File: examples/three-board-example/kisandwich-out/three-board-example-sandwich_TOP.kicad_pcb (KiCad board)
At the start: 6 copper layers, 55 x 55.8 mm, 1 part, among them U2 LM555xM

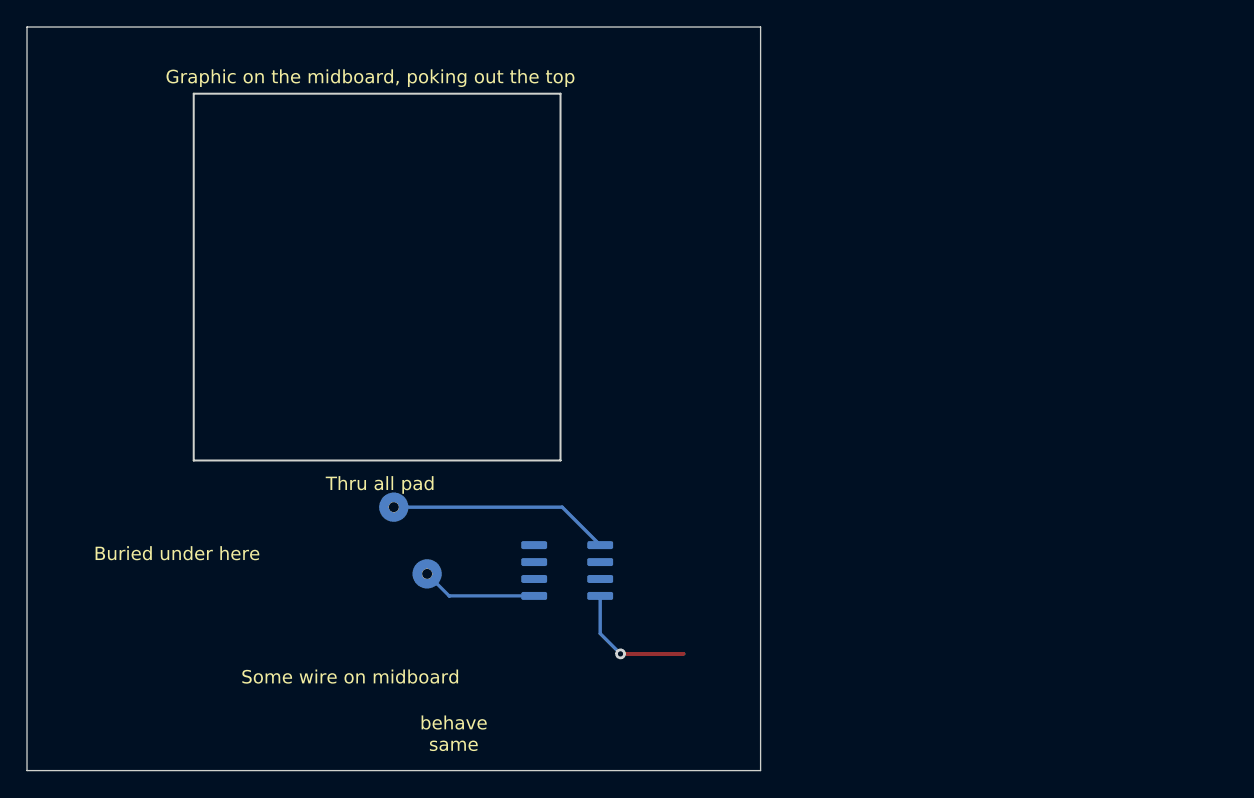
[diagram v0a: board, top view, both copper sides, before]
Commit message: Made 3D representations. Changed speaker to being placed on midboard. Checked heights
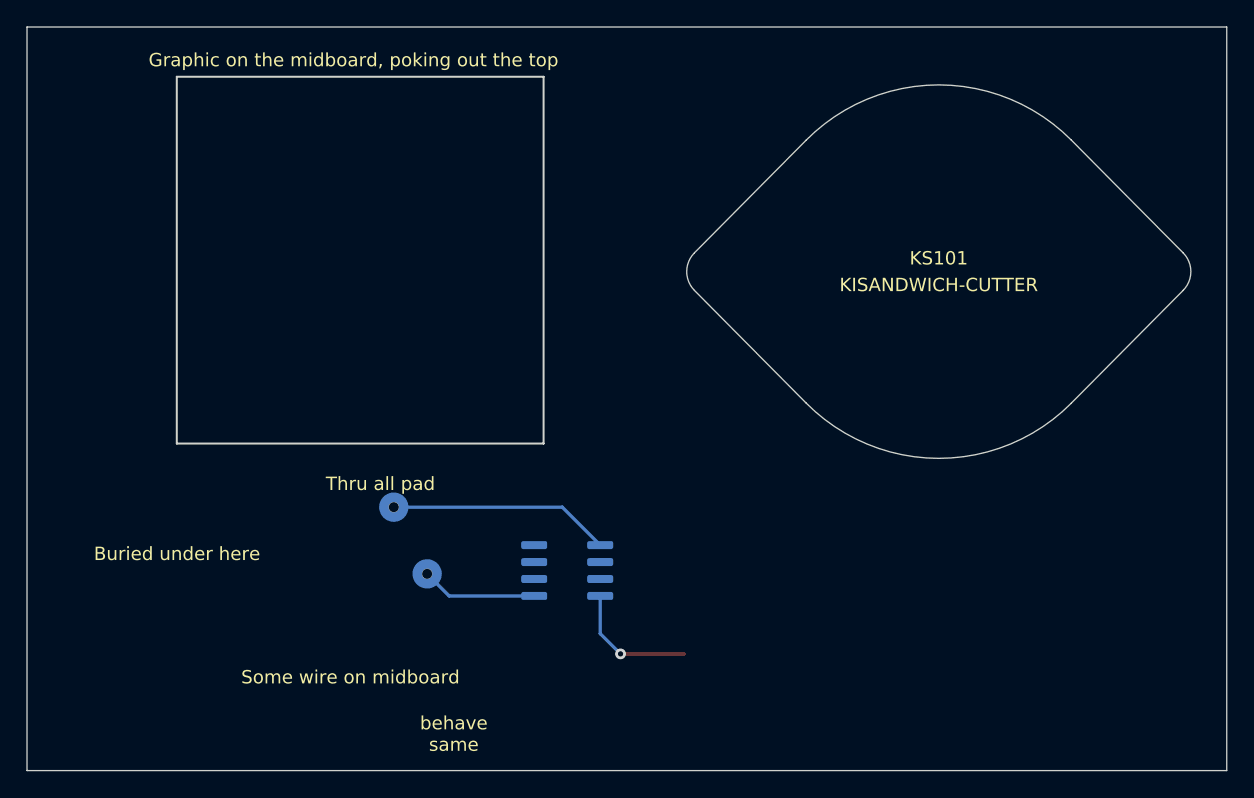
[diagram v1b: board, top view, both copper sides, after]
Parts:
- added KS101: KISANDWICH-CUTTER, Alex_Connectors:CUI-speaker-3layer-tight, F.Cu at (213.4, 53.3)
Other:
- board size 55 x 55.8 mm -> 89.9 x 55.8 mm
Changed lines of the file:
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@@
     (tracks 10)
     (zones 0)
-    (modules 1)
+    (modules 2)
     (nets 9)
   )
@@
     (add_net "Net-(U2-Pad8)")
   )
+  (module Alex_Connectors:CUI-speaker-3layer-tight (layer F.Cu)
+    (at 213.36 53.34 180)
+    (descr "STD_v2_allSketches StepUp generated footprint")
+    (attr smd)
+    (fp_text reference KS101 (at 0 1) (layer F.SilkS)
+      (effects (font (size 1 1) (thickness 0.15)))
+    )
+    (fp_text value KISANDWICH-CUTTER (at 0 -1) (layer F.SilkS)
+      (effects (font (size 1 1) (thickness 0.15)))
+    )
+    (fp_line (start 18.32 -1.408) (end 9.941 -9.858) (layer Edge.Cuts) (width 0.1))
+    (fp_line (start 18.32 1.408) (end 9.941 9.858) (layer Edge.Cuts) (width 0.1))
+    (fp_line (start -18.32 1.408) (end -9.941 9.858) (layer Edge.Cuts) (width 0.1))
+    (fp_line (start -18.32 -1.408) (end -9.941 -9.858) (layer Edge.Cuts) (width 0.1))
+    (fp_text user %R (at 0 1) (layer F.Fab)
+      (effects (font (size 1 1) (thickness 0.15)))
+    )
+    (fp_text user "EDIT PAD NUMBERS" (at 0 -2) (layer Cmts.User)
+      (effects (font (size 1 1) (thickness 0.2) italic))
+    )
+    (fp_arc (start 0 0) (end -9.941 9.858) (angle -90.48) (layer Edge.Cuts) (width 0.1))
+    (fp_arc (start -16.9 0) (end -18.32 -1.408) (angle -89.521) (layer Edge.Cuts) (width 0.1))
+    (fp_arc (start 0 0) (end 9.941 -9.858) (angle -90.479) (layer Edge.Cuts) (width 0.1))
+    (fp_arc (start 16.9 0) (end 18.32 1.408) (angle -89.521) (layer Edge.Cuts) (width 0.1))
+  )
   (module Package_SO:SOIC-8_3.9x4.9mm_P1.27mm (layer B.Cu)
     (at 185.5 75.75)
@@
     (effects (font (size 1 1) (thickness 0.15)))
   )
-  (gr_text "Graphic on the midboard, poking out the top" (at 170.75 38.75) (layer F.SilkS)
+  (gr_text "Graphic on the midboard, poking out the top" (at 169.48 37.48) (layer F.SilkS)
     (effects (font (size 1 1) (thickness 0.15)))
   )
@@
     (effects (font (size 1 1) (thickness 0.15)))
   )
-  (gr_line (start 157.5 40) (end 157.5 67.5) (layer Edge.Cuts) (width 0.15))
-  (gr_line (start 185 40) (end 157.5 40) (layer Edge.Cuts) (width 0.15))
-  (gr_line (start 185 67.5) (end 185 40) (layer Edge.Cuts) (width 0.15))
-  (gr_line (start 157.5 67.5) (end 185 67.5) (layer Edge.Cuts) (width 0.15))
+  (gr_line (start 156.23 38.73) (end 156.23 66.23) (layer Edge.Cuts) (width 0.15))
+  (gr_line (start 183.73 38.73) (end 156.23 38.73) (layer Edge.Cuts) (width 0.15))
+  (gr_line (start 183.73 66.23) (end 183.73 38.73) (layer Edge.Cuts) (width 0.15))
+  (gr_line (start 156.23 66.23) (end 183.73 66.23) (layer Edge.Cuts) (width 0.15))
   (gr_line (start 145 90.75) (end 145 35) (layer Edge.Cuts) (width 0.05))
-  (gr_line (start 200 90.75) (end 145 90.75) (layer Edge.Cuts) (width 0.05))
-  (gr_line (start 200 35) (end 200 90.75) (layer Edge.Cuts) (width 0.05))
-  (gr_line (start 145 35) (end 200 35) (layer Edge.Cuts) (width 0.05))
+  (gr_line (start 234.95 90.75) (end 145 90.75) (layer Edge.Cuts) (width 0.05))
+  (gr_line (start 234.95 35) (end 234.95 90.75) (layer Edge.Cuts) (width 0.05))
+  (gr_line (start 145 35) (end 234.95 35) (layer Edge.Cuts) (width 0.05))
   (via (at 172.5 71) (size 0.7875) (drill 0.75) (layers F.Cu B.Cu) (net 1))
   (segment (start 185.13 71) (end 187.975 73.845) (width 0.25) (layer B.Cu) (net 1))

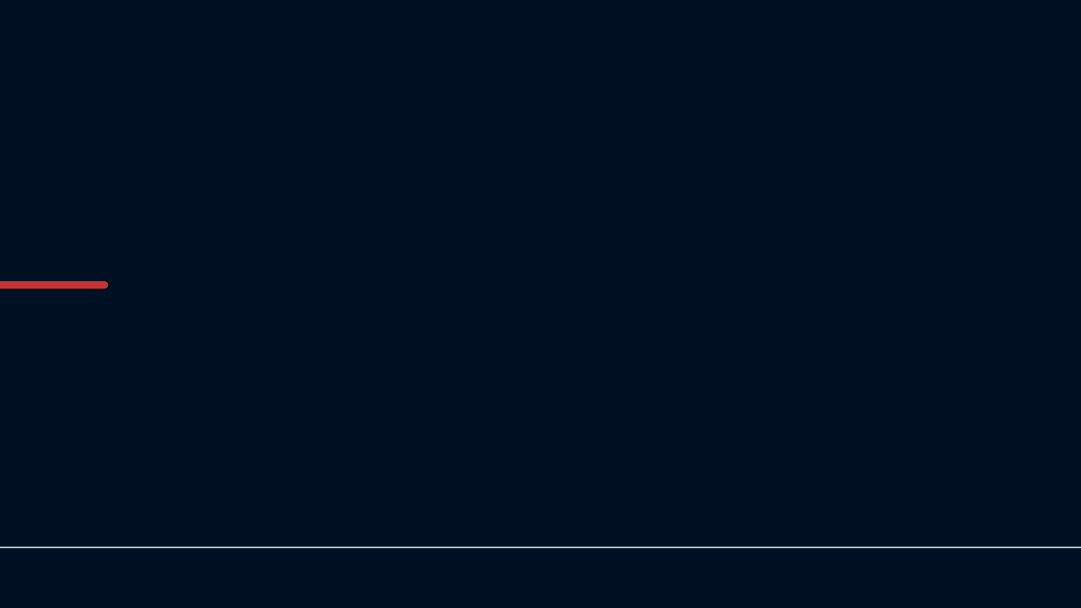
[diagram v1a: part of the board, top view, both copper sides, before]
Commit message: Also processing copper that is in cutter modules
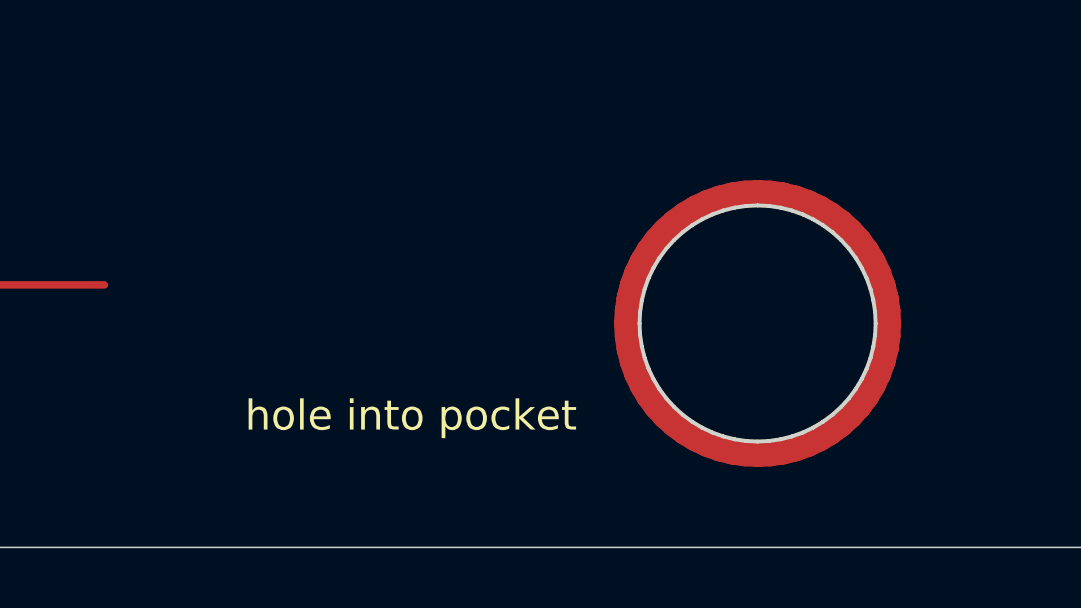
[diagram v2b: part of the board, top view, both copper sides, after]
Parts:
- added svg2mod: KISANDWICH-CUTTER, Alex_Sandwiches:light-hole, F.Cu at (201.9, 77.5)
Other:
- board text added: "hole into pocket"
